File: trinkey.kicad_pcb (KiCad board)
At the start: 2 copper layers, 48.1 x 17.5 mm, 30 parts, among them J1 USB_A, SW1 SW_Push_45deg, U1 RP2040, U2 AMS1117-3.3, U3 W25Q128JVS, X1 ABM8-272-T3

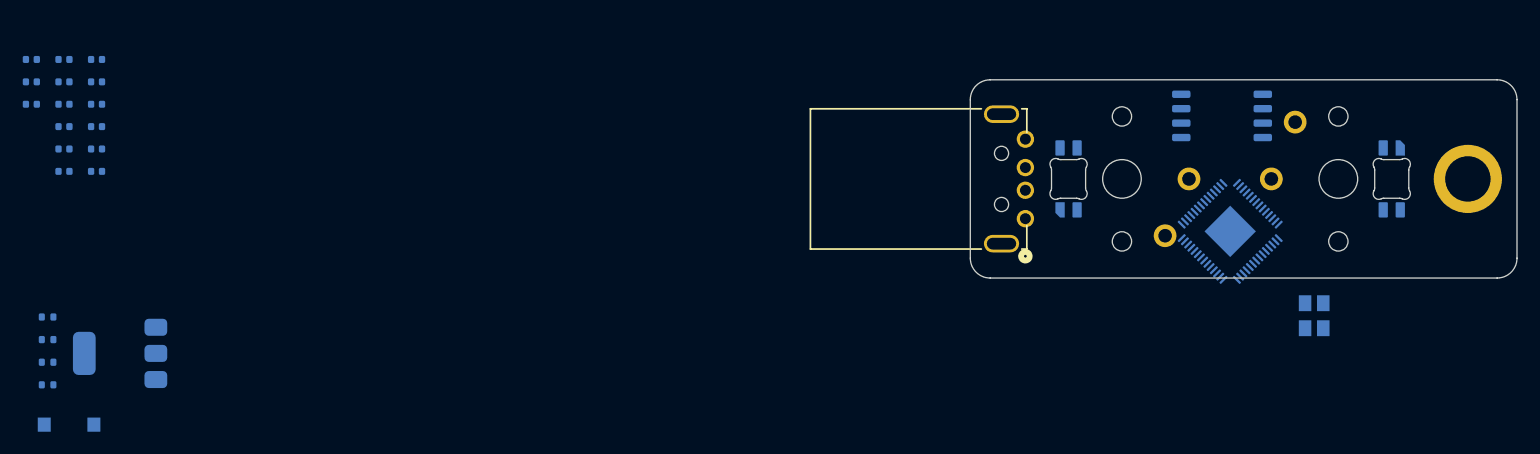
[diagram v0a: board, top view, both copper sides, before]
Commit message: feat: switch to the STM32
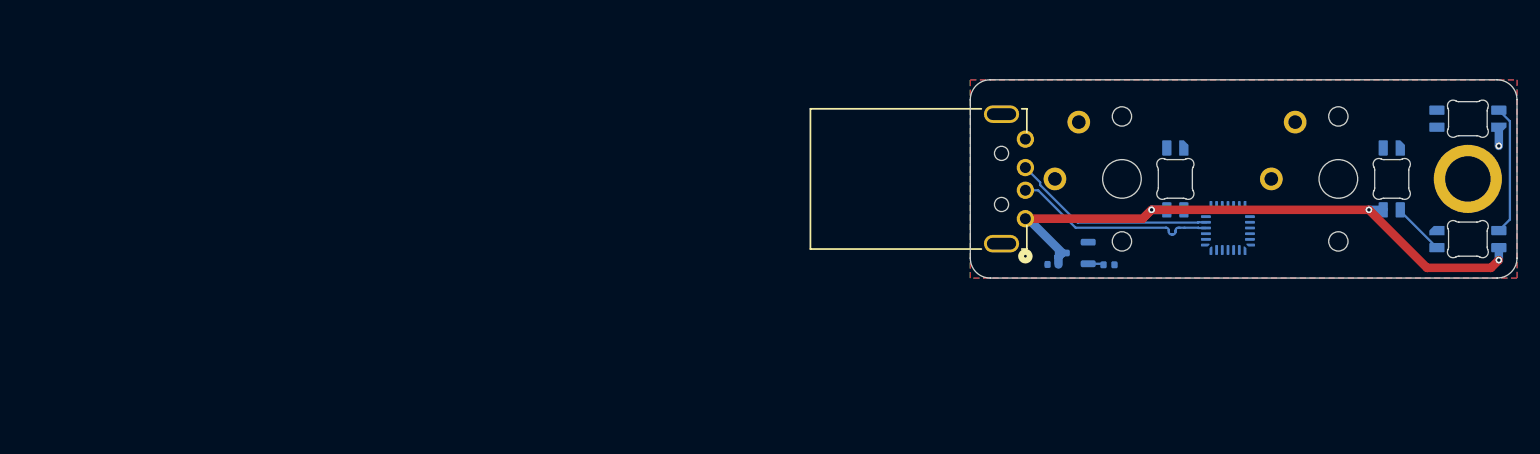
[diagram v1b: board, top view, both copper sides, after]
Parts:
- removed C10, C11, C3, C4, C5, C6, C7, C8, C9: 100n, Capacitor_SMD:C_0402_1005Metric
- removed C12, C13: 1u, Capacitor_SMD:C_0402_1005Metric
- removed C14, C15: 15p, Capacitor_SMD:C_0402_1005Metric
- removed R1, R2: 27.4, Resistor_SMD:R_0402_1005Metric
- removed R3, R4: 1k, Resistor_SMD:R_0402_1005Metric
- removed SW1: SW_Push_45deg, TS-1088-AR02016:SW_TS-1088_XNP-L
- removed U3: W25Q128JVS, Package_SO:SOIC-8_5.3x5.3mm_P1.27mm
- removed X1: ABM8-272-T3, ABM8-272-T3:ABM8-272-T3_ABR
- added LED3: SK6812MINI-E, PCM_marbastlib-various:LED_6028R, B.Cu at (167.4, 30.8)
- added LED4: SK6812MINI-E, PCM_marbastlib-various:LED_6028R, B.Cu at (167.4, 20.2)
- C1, C2: value 10u -> 1u
- U1: value RP2040 -> STM32C071G8Ux; footprint Package_DFN_QFN:QFN-56-1EP_7x7mm_P0.4mm_EP3.2x3.2mm -> Package_DFN_QFN:QFN-28_4x4mm_P0.5mm
- U2: value AMS1117-3.3 -> XC6206PxxxMR; footprint Package_TO_SOT_SMD:SOT-223-3_TabPin2 -> Package_TO_SOT_SMD:SOT-23-3
- moved C2 90.6 mm to (135.9, 33.1), turned to 0 degrees
- moved C1 86.1 mm to (130.9, 33.0)
- moved U2 84.5 mm to (132.9, 32.0)
- moved LED1 9.40 mm to (141.7, 25.5), turned to 90 degrees
- moved U1 0.36 mm to (146.3, 29.8), turned to 180 degrees
- turned CH1 to -90 degrees
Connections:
- LED1 pad 1: +3V3 -> VBUS
- LED2 pad 1: +3V3 -> VBUS
- LED2 pad 2: unconnected-(LED2-DOUT-Pad2) -> Net-(LED2-DOUT)
- U1 pad 1: +3V3 -> unconnected-(U1-PC14-Pad1)
- U1 pad 10: +3V3 -> unconnected-(U1-PA4-Pad10)
- U1 pad 18: unconnected-(U1-GPIO15-Pad18) -> /D-
- U1 pad 19: unconnected-(U1-TESTEN-Pad19) -> /D+
- U1 pad 20: Net-(U1-XIN) -> unconnected-(U1-PA13-Pad20)
- U1 pad 21: Net-(U1-XOUT) -> unconnected-(U1-PA14-Pad21)
- U1 pad 22: +3V3 -> unconnected-(U1-PA15-Pad22)
- U1 pad 23: +1V1 -> unconnected-(U1-PB3-Pad23)
- U1 pad 3: unconnected-(U1-GPIO1-Pad3) -> +3V3
- U1 pad 4: unconnected-(U1-GPIO2-Pad4) -> GND
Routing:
- net VBUS: track 0.00 -> 53.8 mm, vias 0 -> 3
- net /D+: track 0.00 -> 18.3 mm
- net /D-: track 0.00 -> 18.0 mm
- net Net-(LED3-DOUT): track 0.00 -> 11.4 mm
- net Net-(LED2-DOUT): track 0.00 -> 4.66 mm
- net GND: track 0.00 -> 1.64 mm, vias 0 -> 1
- net +3V3: track 0.00 -> 1.39 mm
- added copper zone on B.Cu, net GND
- added copper zone on F.Cu, net GND

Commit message: feat: polishing and readme
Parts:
- removed REF**: MountingHole_4mm_Pad, MountingHole:MountingHole_4mm_Pad
- added C3: 100n, Capacitor_SMD:C_0402_1005Metric, B.Cu at (149.9, 29.1)
- added C4: 4.7u, Capacitor_SMD:C_0402_1005Metric, B.Cu at (150.4, 30.5)
- added C5: 10u, Capacitor_SMD:C_0402_1005Metric, B.Cu at (157.3, 28.2)
- added C6: 100n, Capacitor_SMD:C_0402_1005Metric, B.Cu at (163.2, 20.8)
- added C7: 100n, Capacitor_SMD:C_0402_1005Metric, B.Cu at (162.7, 32.3)
- added C8: 100n, Capacitor_SMD:C_0402_1005Metric, B.Cu at (159.5, 29.8)
- added C9: 100n, Capacitor_SMD:C_0402_1005Metric, B.Cu at (138.8, 23.1)
- added R1: 47, Resistor_SMD:R_0402_1005Metric, B.Cu at (145.8, 20.4)
- added TP1: SWDIO, TestPoint:TestPoint_Pad_D1.0mm, B.Cu at (139.4, 20.0)
- added TP2: SWCLK, TestPoint:TestPoint_Pad_D1.0mm, B.Cu at (144.4, 20.0)
- added TP3: NRST, TestPoint:TestPoint_Pad_D1.0mm, B.Cu at (152.8, 30.9)
- added TP4: 3V3, TestPoint:TestPoint_Pad_D1.0mm, B.Cu at (152.8, 27.2)
- added TP5: GND, TestPoint:TestPoint_Pad_D1.0mm, B.Cu at (149.4, 20.0)
- added U3: USBLC6-2SC6, Package_TO_SOT_SMD:SOT-23-6, B.Cu at (132.9, 28.6)
- added U4: 74AHCT1G125, Package_TO_SOT_SMD:SOT-23-5, B.Cu at (146.9, 23.0)
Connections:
- CH1 pad 1: unconnected-(CH1-Pad1) -> GND
- CH1 pad 2: GND -> /SW1
- CH2 pad 1: unconnected-(CH2-Pad1) -> GND
- CH2 pad 2: GND -> /SW2
- J1 pad 2: /D- -> Net-(J1-D-)
- J1 pad 3: /D+ -> Net-(J1-D+)
- LED1 pad 3: unconnected-(LED1-DIN-Pad3) -> Net-(LED1-DIN)
- U1 pad 1: unconnected-(U1-PC14-Pad1) -> /SW2
- U1 pad 20: unconnected-(U1-PA13-Pad20) -> /SW1
- U1 pad 21: unconnected-(U1-PA14-Pad21) -> /SWCLK
- U1 pad 24: unconnected-(U1-PB4-Pad24) -> /LED_DATA
- U1 pad 5: unconnected-(U1-PF2-Pad5) -> /NRST
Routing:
- net VBUS: track 53.8 -> 99.3 mm, vias 3 -> 5
- net +3V3: track 1.39 -> 26.1 mm
- net /SW1: track 0.00 -> 23.4 mm
- net Net-(LED1-DOUT): track 0.00 -> 20.1 mm, vias 0 -> 2
- net /SWCLK: track 0.00 -> 9.02 mm, vias 0 -> 2
- net /D+: track 18.3 -> 11.3 mm
- net Net-(LED1-DIN): track 0.00 -> 6.90 mm
- net /D-: track 18.0 -> 11.2 mm
- net /LED_DATA: track 0.00 -> 6.50 mm
- net Net-(J1-D-): track 0.00 -> 4.82 mm
- net /NRST: track 0.00 -> 4.79 mm, vias 0 -> 2
- net Net-(J1-D+): track 0.00 -> 4.74 mm
- net Net-(R1-Pad1): track 0.00 -> 4.08 mm
- net /SW2: track 0.00 -> 3.57 mm
- net GND: track 1.64 -> 4.89 mm, vias 1 -> 6
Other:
- outline, holes or cut-outs redrawn
